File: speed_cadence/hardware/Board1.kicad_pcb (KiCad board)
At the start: 2 copper layers, 8.6 x 5 mm, 6 parts, among them IC1 AH1912-W-7, J1 DX07S016JA3R1500, SW1 SW_Push, U1 STM32F042G6U6TR, U2 TS2940CW33_RPG

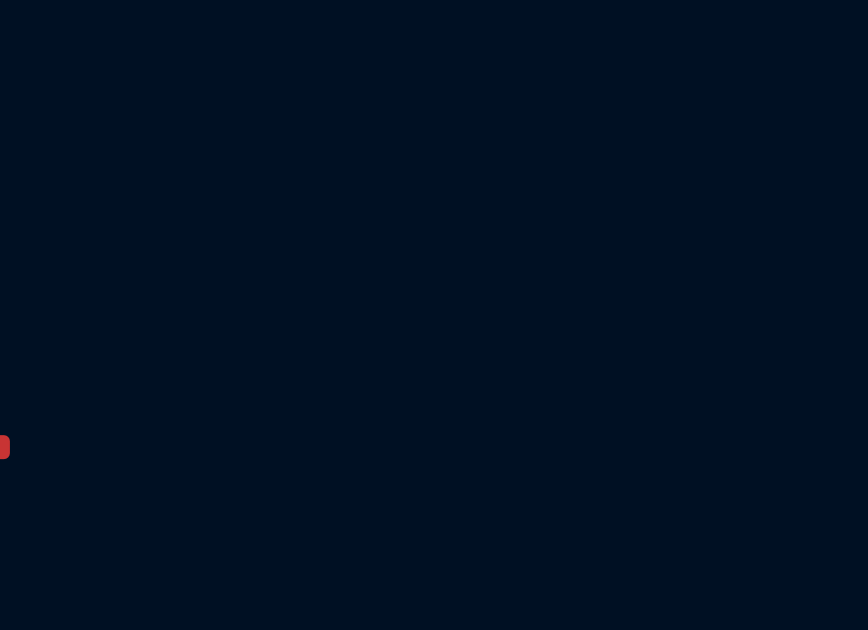
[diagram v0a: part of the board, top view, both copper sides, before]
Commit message: Added footprints for capacitors
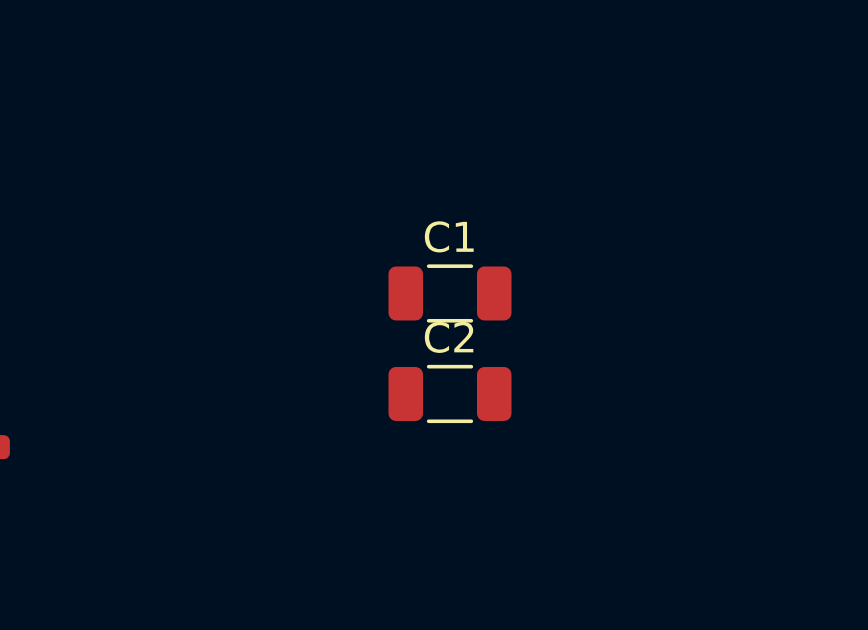
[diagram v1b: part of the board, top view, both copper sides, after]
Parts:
- added C1: 0.47u, Capacitor_SMD:C_1206_3216Metric, F.Cu at (89.7, 37.4)
- added C2: 22u, Capacitor_SMD:C_1206_3216Metric, F.Cu at (89.7, 40.8)
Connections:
- IC1 pad 1: VDD -> +5V
- IC1 pad 3: GND -> +3V3
- J1 pad 1: unconnected-(J1-GND-Pad1) -> +3V3
- J1 pad 12: unconnected-(J1-GND-Pad12) -> +3V3
- R1 pad 1: VDD -> +5V
- SW1 pad 2: GND -> +3V3
- U1 pad 16: GND -> +3V3
- U1 pad 17: VDD -> +3V3
- U2 pad 1: unconnected-(U2-INPUT-Pad1) -> +5V
- U2 pad 2: unconnected-(U2-GROUND_1-Pad2) -> +3V3
- U2 pad 3: unconnected-(U2-OUTPUT-Pad3) -> Net-(U2-OUTPUT)

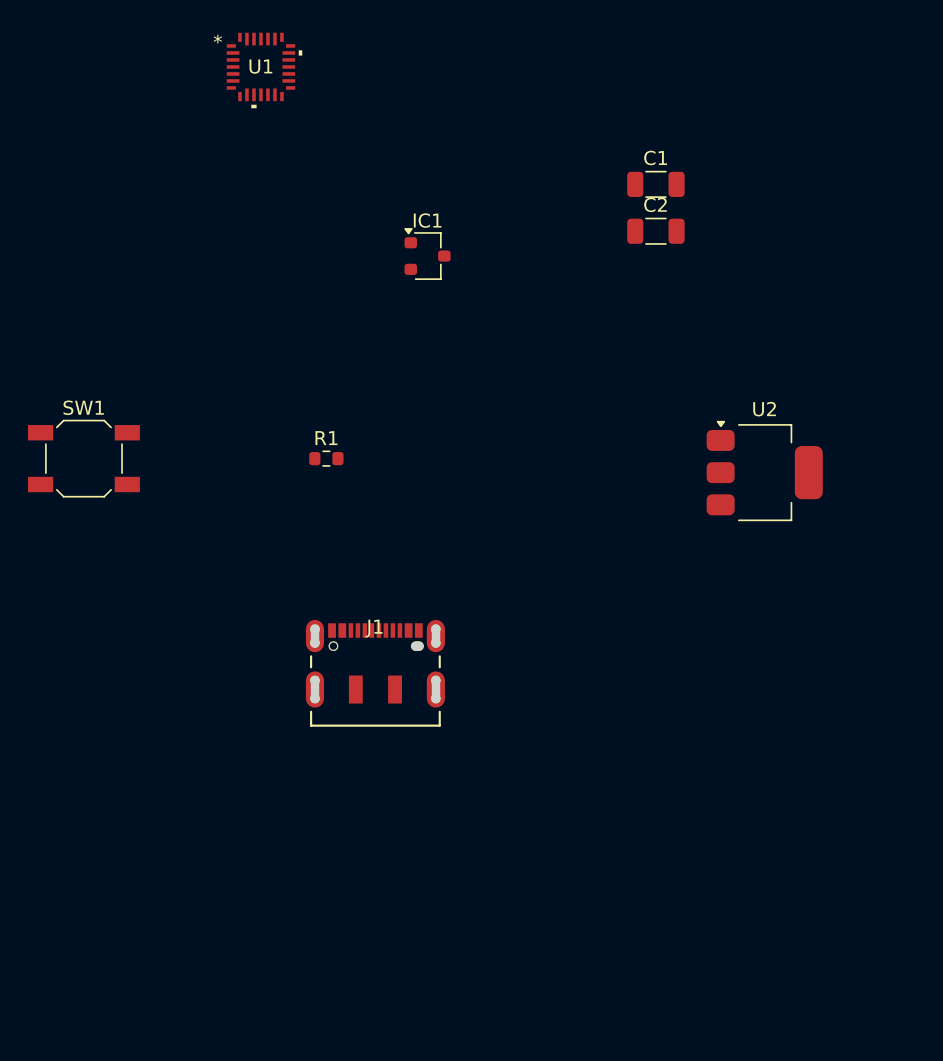
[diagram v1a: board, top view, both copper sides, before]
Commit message: Fixed power outputs
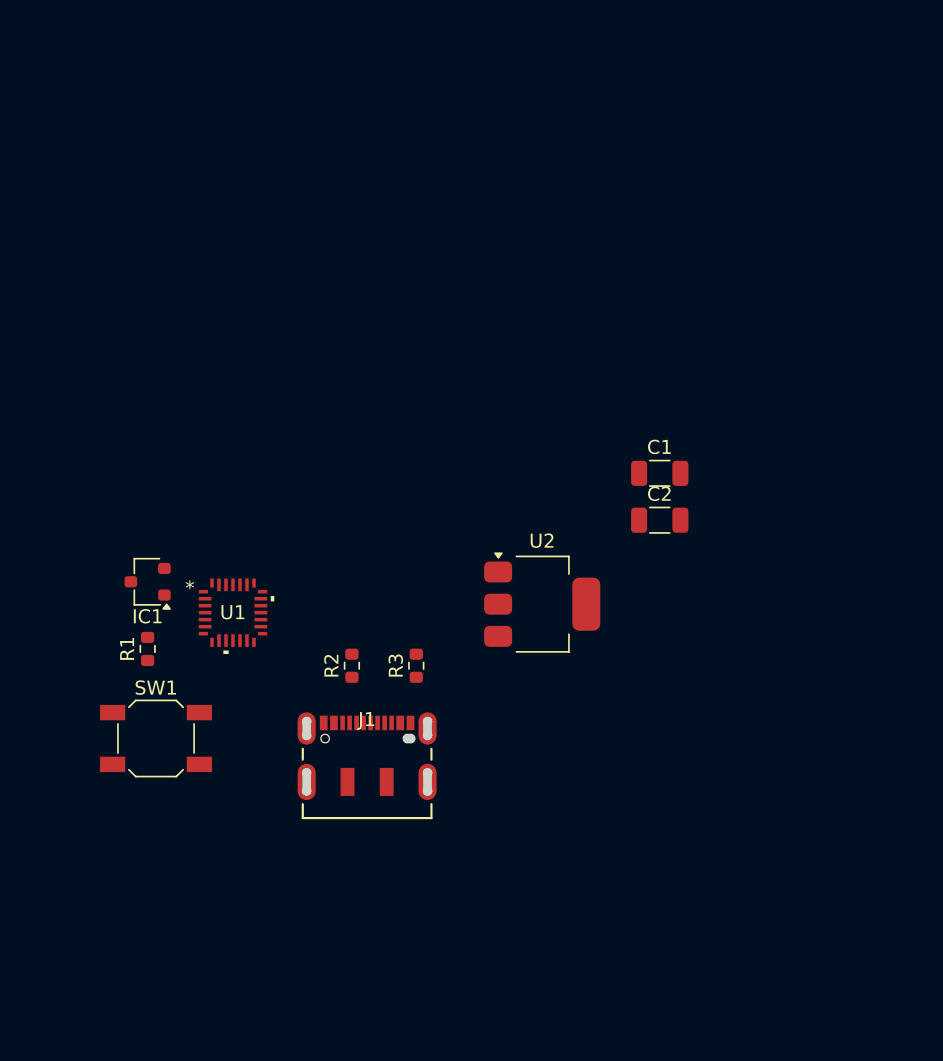
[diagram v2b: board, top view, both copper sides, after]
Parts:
- added R2: 5.1k, Resistor_SMD:R_0603_1608Metric, F.Cu at (68.0, 71.8)
- added R3: 5.1k, Resistor_SMD:R_0603_1608Metric, F.Cu at (72.6, 71.8)
- moved U1 39.1 mm to (59.5, 68.0)
- moved IC1 30.7 mm to (53.4, 65.8), turned to 180 degrees
- moved SW1 20.7 mm to (54.0, 77.0)
- moved C1 20.7 mm to (90.0, 58.0)
- moved C2 20.7 mm to (90.0, 61.4)
- moved R1 18.7 mm to (53.4, 70.6), turned to 90 degrees
- moved U2 18.5 mm to (81.6, 67.4)
- moved J1 6.63 mm to (69.1, 79.1)
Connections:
- C1 pad 2: +3V3 -> GND
- C2 pad 1: Net-(U2-OUTPUT) -> 3V3
- C2 pad 2: +3V3 -> GND
- IC1 pad 3: +3V3 -> GND
- J1 pad 1: +3V3 -> GND
- J1 pad 11: unconnected-(J1-VBUS-Pad11) -> +5V
- J1 pad 12: +3V3 -> GND
- J1 pad 2: unconnected-(J1-VBUS-Pad2) -> +5V
- J1 pad 3: unconnected-(J1-CC1-Pad3) -> Net-(J1-CC1)
- J1 pad 5: unconnected-(J1-D--Pad5) -> Net-(U1A-PA9/PA11)
- J1 pad 6: unconnected-(J1-D+-Pad6) -> Net-(U1A-PA10/PA12)
- J1 pad 7: unconnected-(J1-D+-Pad7) -> Net-(U1A-PA10/PA12)
- J1 pad 8: unconnected-(J1-D--Pad8) -> Net-(U1A-PA9/PA11)
- J1 pad 9: unconnected-(J1-CC2-Pad9) -> Net-(J1-CC2)
- SW1 pad 2: +3V3 -> GND
- U1 pad 16: +3V3 -> GND
- U1 pad 17: +3V3 -> 3V3
- U1 pad 19: unconnected-(U1A-PA9/PA11-Pad19) -> Net-(U1A-PA9/PA11)
- U1 pad 20: unconnected-(U1A-PA10/PA12-Pad20) -> Net-(U1A-PA10/PA12)
- U2 pad 2: +3V3 -> GND
- U2 pad 3: Net-(U2-OUTPUT) -> 3V3

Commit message: Preliminary PCB placement
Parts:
- moved R1 42.5 mm to (95.0, 79.2), turned to -90 degrees
- moved SW1 40.1 mm to (93.0, 86.2), turned to -90 degrees
- moved IC1 33.3 mm to (78.2, 88.0), turned to 0 degrees
- moved U1 25.9 mm to (83.0, 79.0)
- moved J1 19.1 mm to (81.3, 64.5), turned to 180 degrees
- moved R2 16.4 mm to (84.4, 71.8), turned to 0 degrees
- moved C1 15.0 mm to (90.4, 73.0), turned to 180 degrees
- moved C2 12.9 mm to (95.6, 73.0)
- moved U2 11.6 mm to (93.0, 65.2), turned to 90 degrees
- moved R3 5.40 mm to (78.0, 71.6), turned to 180 degrees
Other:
- outline, holes or cut-outs redrawn

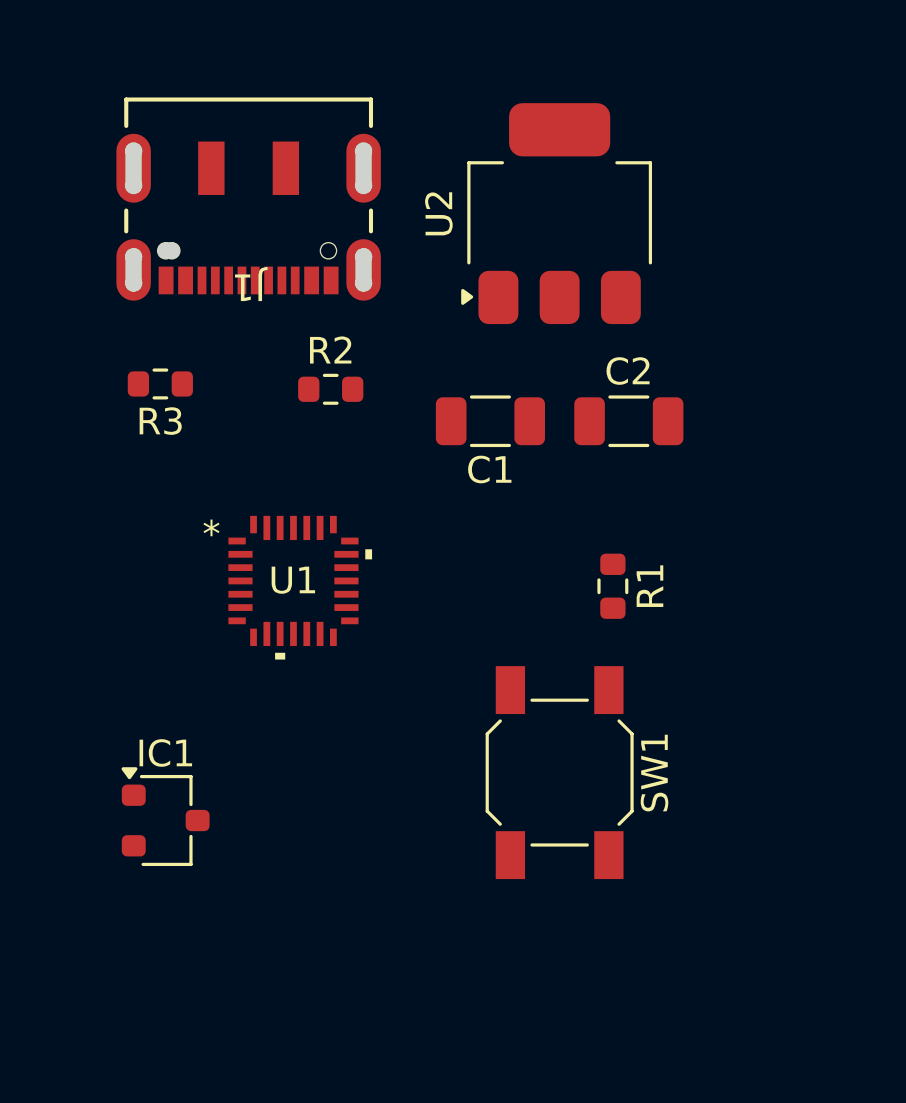
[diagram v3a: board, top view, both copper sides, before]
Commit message: Added final pins and finished physical layout
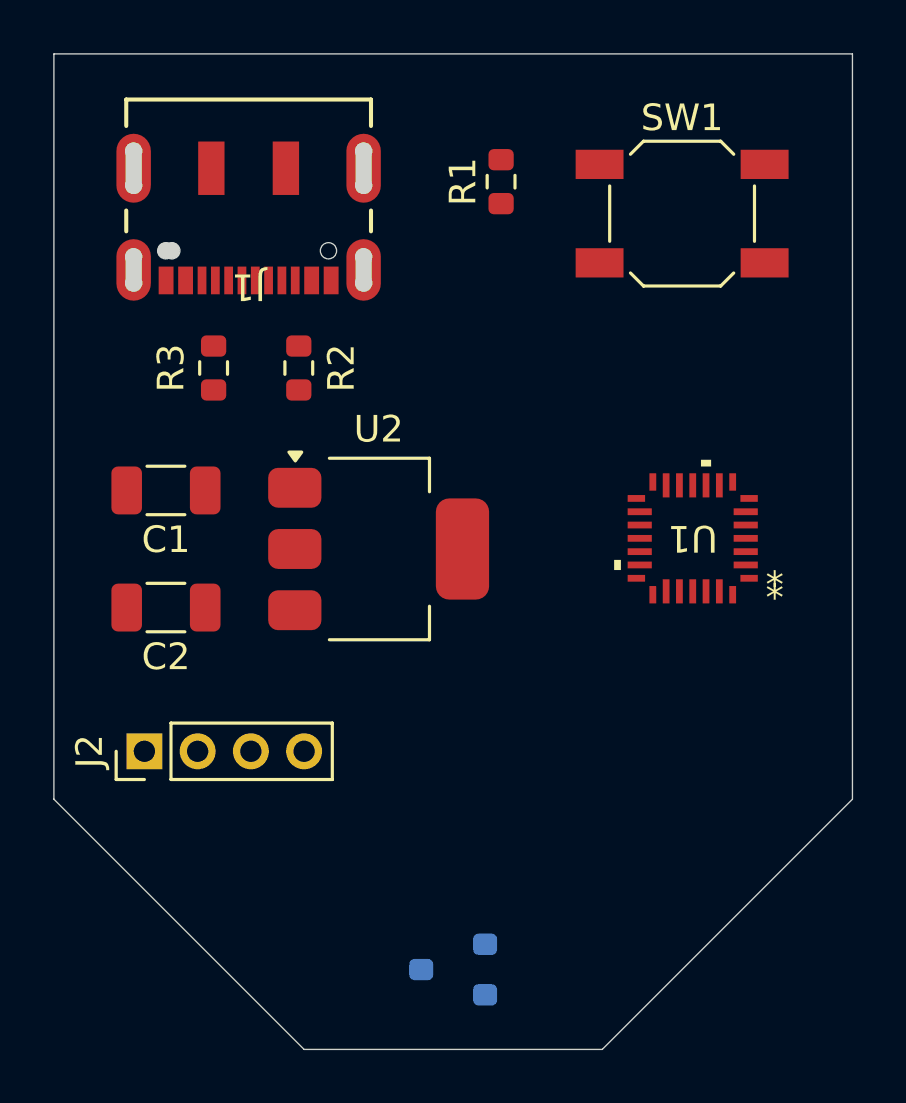
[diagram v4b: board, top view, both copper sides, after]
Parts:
- added J2: Conn_01x04_Pin, Connector_PinHeader_2.00mm:PinHeader_1x04_P2.00mm_Vertical, F.Cu at (77.4, 85.4)
- IC1: moved to B.Cu
- moved SW1 21.5 mm to (97.6, 65.2), turned to 0 degrees
- moved C2 18.7 mm to (78.2, 80.0), turned to 180 degrees
- moved R1 15.8 mm to (90.8, 64.0), turned to 90 degrees
- moved U1 15.1 mm to (98.0, 77.4), turned to 180 degrees
- moved U2 14.3 mm to (86.2, 77.8), turned to 0 degrees
- moved C1 12.5 mm to (78.2, 75.6)
- moved IC1 12.2 mm to (89.0, 93.6), turned to 180 degrees
- moved R3 2.09 mm to (80.0, 71.0), turned to -90 degrees
- moved R2 1.44 mm to (83.2, 71.0), turned to -90 degrees
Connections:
- net 3V3 renamed +3V3
- net Net-(U1A-PA10/PA12) renamed CAN_TX
- net Net-(U1A-PA9/PA11) renamed CAN_RX
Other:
- board size 8.6 x 5 mm -> 30 x 37.4 mm

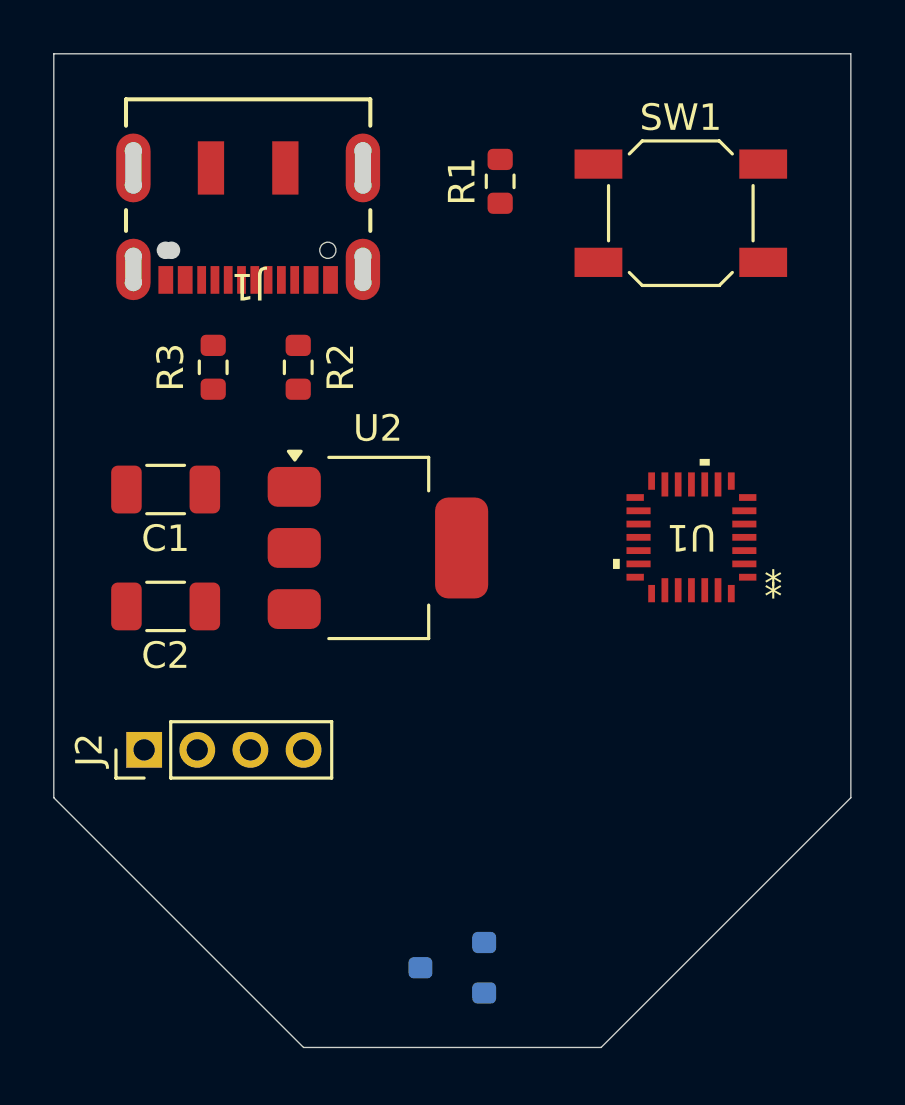
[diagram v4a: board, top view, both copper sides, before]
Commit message: Added the tracks and tried fixing the outline but didn’t work for some reason, even if it is a polygon. I think it doesn’t like that its angled...
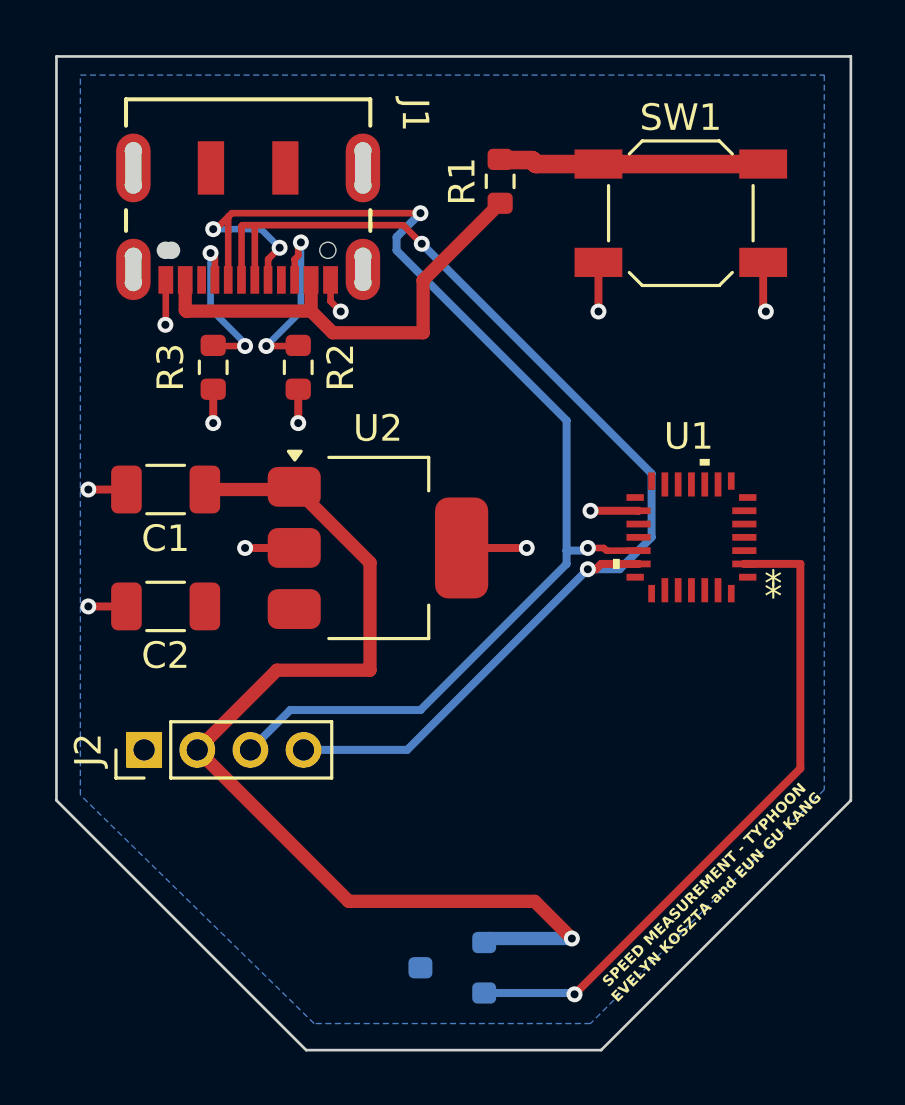
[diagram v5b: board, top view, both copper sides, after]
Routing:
- net +5V: track 0.00 -> 57.3 mm, vias 0 -> 1
- net CAN_RX: track 0.00 -> 48.5 mm, vias 0 -> 4
- net CAN_TX: track 0.00 -> 44.2 mm, vias 0 -> 2
- net Net-(IC1-OUTPUT): track 0.00 -> 25.3 mm, vias 0 -> 1
- net GND: track 0.00 -> 18.3 mm, vias 0 -> 11
- net Net-(U1A-NRST): track 0.00 -> 10.2 mm
- net Net-(J1-CC1): track 0.00 -> 7.40 mm, vias 0 -> 2
- net Net-(J1-CC2): track 0.00 -> 6.43 mm, vias 0 -> 2
- added copper zone on B.Cu, net GND
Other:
- board size 30 x 37.4 mm -> 29.9 x 37.4 mm
- board text added: "SPEED MEASUREMENT - TYPHOON EVELYN KOSZTA and EUN GU KANG"

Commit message: Fixed 3.3v and 5v connections to J1
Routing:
- net +3V3: track 0.00 -> 18.4 mm, vias 0 -> 2
- net Net-(U1A-NRST): track 10.2 -> 27.8 mm
- net +5V: track 57.3 -> 65.1 mm
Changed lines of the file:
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@@
+	)
+	(segment
+		(start 92 77.1)
+		(end 91.2 76.3)
+		(width 0.25)
+		(layer "F.Cu")
+		(net 9)
+	)
+	(segment
+		(start 83.05 80.1)
+		(end 84.8 80.1)
+		(width 0.5)
+		(layer "F.Cu")
+		(net 9)
+	)
+	(segment
+		(start 94.899999 76.900001)
+		(end 94.7 77.1)
+		(width 0.25)
+		(layer "F.Cu")
+		(net 9)
+	)
+	(segment
+		(start 79.6843 80)
+		(end 82.95 80)
+		(width 0.5)
+		(layer "F.Cu")
+		(net 9)
+	)
+	(segment
+		(start 82.95 80)
+		(end 83.05 80.1)
+		(width 0.5)
+		(layer "F.Cu")
+		(net 9)
+	)
+	(segment
+		(start 94.7 77.1)
+		(end 92 77.1)
+		(width 0.25)
+		(layer "F.Cu")
+		(net 9)
+	)
+	(segment
+		(start 96.0093 76.900001)
+		(end 94.899999 76.900001)
+		(width 0.25)
+		(layer "F.Cu")
+		(net 9)
+	)
+	(via
+		(at 84.8 80.1)
+		(size 0.6)
+		(drill 0.3)
+		(layers "F.Cu" "B.Cu")
+		(free yes)
+		(net 9)
+	)
+	(via
+		(at 91.2 76.3)
+		(size 0.6)
+		(drill 0.3)
+		(layers "F.Cu" "B.Cu")
+		(net 9)
+	)
+	(segment
+		(start 84.8 80.1)
+		(end 87.4 80.1)
+		(width 0.5)
+		(layer "B.Cu")
+		(net 9)
+	)
+	(segment
+		(start 87.4 80.1)
+		(end 91.2 76.3)
+		(width 0.5)
+		(layer "B.Cu")
+		(net 9)
 	)
 	(segment
@@
 	)
 	(segment
+		(start 87.9 69.7)
+		(end 87.9 70.65)
+		(width 0.5)
+		(layer "F.Cu")
+		(net 26)
+	)
+	(segment
 		(start 85.9 78.35)
 		(end 83.05 75.5)
@@
 		(start 83.683333 68.883333)
 		(end 79.016667 68.883333)
+		(width 0.5)
+		(layer "F.Cu")
+		(net 26)
+	)
+	(segment
+		(start 87.9 70.65)
+		(end 83.05 75.5)
 		(width 0.5)
 		(layer "F.Cu")
@@
 		(start 94.5 63.35)
 		(end 92.15 63.35)
-		(width 0.7)
+		(width 0.3)
 		(layer "F.Cu")
 		(net 27)
@@
 		(start 100.7 63.35)
 		(end 94.5 63.35)
-		(width 0.7)
+		(width 0.3)
 		(layer "F.Cu")
 		(net 27)
@@
 	)
 	(segment
+		(start 102.5 76.6)
+		(end 102.5 63.8)
+		(width 0.3)
+		(layer "F.Cu")
+		(net 27)
+	)
+	(segment
 		(start 92.15 63.35)
 		(end 92 63.2)
-		(width 0.7)
+		(width 0.3)
+		(layer "F.Cu")
+		(net 27)
+	)
+	(segment
+		(start 101.7 77.4)
+		(end 102.5 76.6)
+		(width 0.3)
+		(layer "F.Cu")
+		(net 27)
+	)
+	(segment
+		(start 102.5 63.8)
+		(end 102.05 63.35)
+		(width 0.3)
 		(layer "F.Cu")
 		(net 27)
@@
 		(start 92 63.2)
 		(end 90.825 63.2)
-		(width 0.7)
-		(layer "F.Cu")
-		(net 27)
+		(width 0.3)
+		(layer "F.Cu")
+		(net 27)
+	)
+	(segment
+		(start 99.9907 77.4)
+		(end 101.7 77.4)
+		(width 0.3)
+		(layer "F.Cu")
+		(net 27)
+	)
+	(segment
+		(start 102.05 63.35)
+		(end 100.7 63.35)
+		(width 0.3)
+		(layer "F.Cu")
+		(net 27)
